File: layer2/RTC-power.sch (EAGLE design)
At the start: 15 parts, among them U1 DS3234, U2 MCP73831

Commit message: Initail board argment
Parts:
- removed C4: 4.7uF, SparkFun-Capacitors:4.7UF-6.3V-10%(0603)0603
- removed R4: 2.0k, SparkFun-Resistors:2.0KOHM1/10W5%(0603)
- added C2: 4.7uF, microbuilder:CAP_CERAMIC0805-NOOUTLINE
- C1: device SparkFun:CAP0402-CAP -> microbuilder:CAP_CERAMIC0805-NOOUTLINE
- C3: device SparkFun-Capacitors:4.7UF-6.3V-10%(0603)0603 -> microbuilder:CAP_CERAMIC0805-NOOUTLINE
- R1: value 10k -> 10K; device SparkFun:RESISTOR0402-RES -> microbuilder:RESISTOR_0805MP
- R2: value (none) -> 2.0k; device SparkFun-Resistors:RESISTORPTH-1/4W-VERT-KIT -> microbuilder:RESISTOR_0805MP
- R3: device SparkFun-Resistors:330OHM1/10W1%(0603) -> microbuilder:RESISTOR_0805MP
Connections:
- removed net VCC: C1.2, R1.1
- net +3V3: now also C1.1, R1.1
- net GND: now also C1.2, C2.2; no longer C1.1, C4.2, R4.2
- net N$3: now also R3.2; no longer R3.1
- net PROG: no longer R4.1
- net VIN: now also C2.1, R3.1; no longer C3.1, R3.2
- net V_RAW: now also C3.1; no longer C4.1
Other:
- moved on the sheet: C1, C3

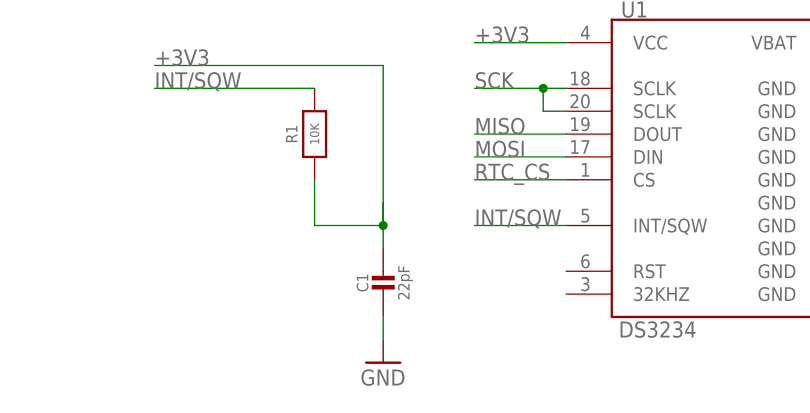
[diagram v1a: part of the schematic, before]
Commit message: layed out all conectons on board
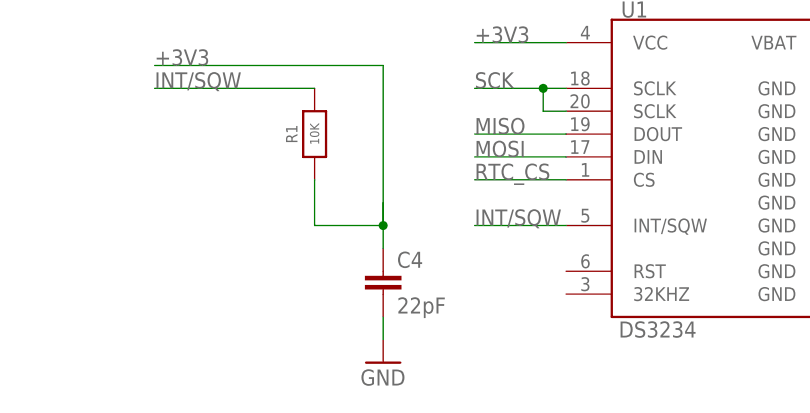
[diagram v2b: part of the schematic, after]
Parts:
- removed C1: 22pF, microbuilder:CAP_CERAMIC0805-NOOUTLINE
- added C4: 22pF, SparkFun:CAP0402-CAP
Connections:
- net +3V3: now also C4.1; no longer C1.1
- net GND: now also C4.2; no longer C1.2
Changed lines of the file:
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@@
 <part name="R3" library="microbuilder" deviceset="RESISTOR" device="_0805MP" value="330"/>
 <part name="R2" library="microbuilder" deviceset="RESISTOR" device="_0805MP" value="2.0k"/>
-<part name="C1" library="microbuilder" deviceset="CAP_CERAMIC" device="0805-NOOUTLINE" value="22pF"/>
 <part name="C2" library="microbuilder" deviceset="CAP_CERAMIC" device="0805-NOOUTLINE" value="4.7uF"/>
 <part name="C3" library="microbuilder" deviceset="CAP_CERAMIC" device="0805-NOOUTLINE" value="4.7uF"/>
+<part name="C4" library="SparkFun" deviceset="CAP" device="0402-CAP" value="22pF"/>
 </parts>
 <sheets>
@@
 <instance part="R3" gate="G$1" x="63.5" y="76.2" rot="R90"/>
 <instance part="R2" gate="G$1" x="93.98" y="76.2" rot="R90"/>
-<instance part="C1" gate="G$1" x="48.26" y="25.4"/>
 <instance part="C2" gate="G$1" x="48.26" y="91.44"/>
 <instance part="C3" gate="G$1" x="104.14" y="91.44"/>
+<instance part="C4" gate="G$1" x="48.26" y="25.4"/>
 </instances>
 <busses>
@@
 </segment>
 <segment>
-<pinref part="C1" gate="G$1" pin="2"/>
 <pinref part="GND2" gate="1" pin="GND"/>
 <wire x1="48.26" y1="22.86" x2="48.26" y2="20.32" width="0.1524" layer="91"/>
+<pinref part="C4" gate="G$1" pin="2"/>
 </segment>
 </net>
@@
 <label x="22.86" y="50.8" size="1.778" layer="95"/>
 <pinref part="R1" gate="G$1" pin="1"/>
-<pinref part="C1" gate="G$1" pin="1"/>
 <wire x1="48.26" y1="30.48" x2="48.26" y2="33.02" width="0.1524" layer="91"/>
-</segment>
-</net>
+<pinref part="C4" gate="G$1" pin="1"/>
+</segment>
+</net>

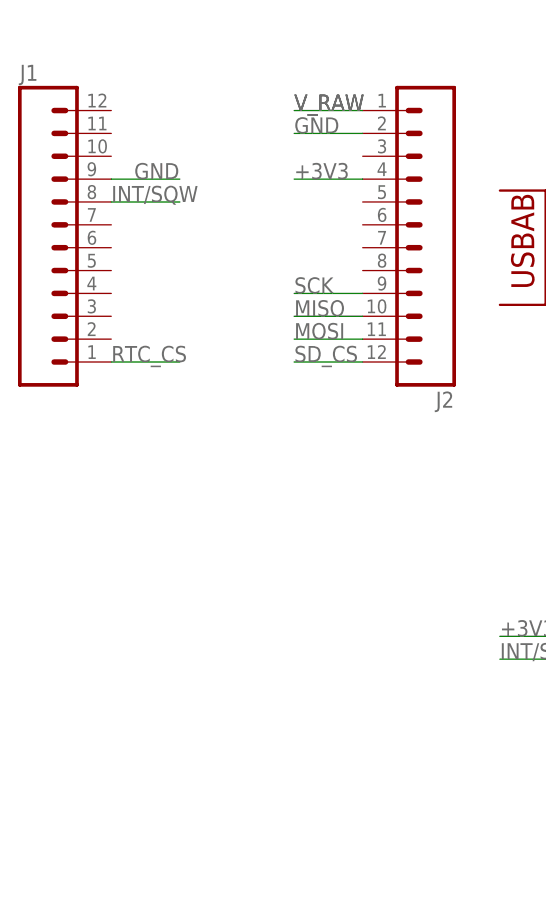
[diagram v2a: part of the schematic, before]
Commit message: removed unneeded header to give battery access
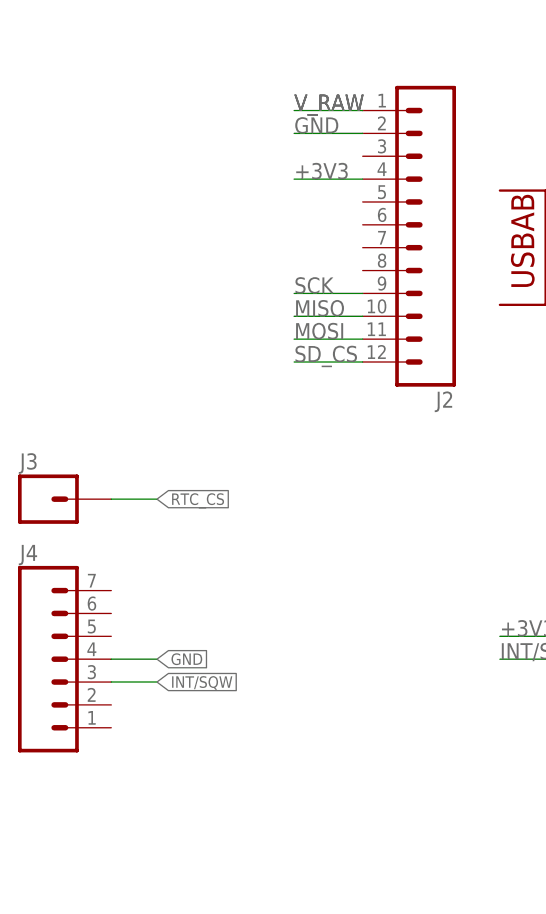
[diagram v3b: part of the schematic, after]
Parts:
- removed J1: (no value), SparkFun-Connectors:M12PTH
- added J3: (no value), SparkFun-Connectors:M01PTH
- added J4: (no value), SparkFun-Connectors:M07
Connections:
- net GND: now also J4.4; no longer J1.9
- net INT/SQW: now also J4.3; no longer J1.8
- net RTC_CS: now also J3.1; no longer J1.1
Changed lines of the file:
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@@
 <setting verticaltext="up"/>
 </settings>
-<grid distance="0.1" unitdist="inch" unit="inch" style="lines" multiple="1" display="no" altdistance="0.01" altunitdist="inch" altunit="inch"/>
+<grid distance="0.1" unitdist="inch" unit="inch" style="lines" multiple="1" display="yes" altdistance="0.01" altunitdist="inch" altunit="inch"/>
 <layers>
 <layer number="1" name="Top" color="4" fill="1" visible="no" active="no"/>
@@
 <part name="JP9" library="SparkFun-Connectors" deviceset="USB-AB" device="CONN-11794" value="Micro USB"/>
 <part name="JP1" library="SparkFun-Connectors" deviceset="JST_2MM_MALE" device="" value="JST"/>
-<part name="J1" library="SparkFun-Connectors" deviceset="M12" device="PTH"/>
 <part name="J2" library="SparkFun-Connectors" deviceset="M12" device="PTH"/>
 <part name="R1" library="microbuilder" deviceset="RESISTOR" device="_0805MP" value="10K"/>
@@
 <part name="C3" library="microbuilder" deviceset="CAP_CERAMIC" device="0805-NOOUTLINE" value="4.7uF"/>
 <part name="C4" library="SparkFun" deviceset="CAP" device="0402-CAP" value="22pF"/>
+<part name="J3" library="SparkFun-Connectors" deviceset="M01" device="PTH"/>
+<part name="J4" library="SparkFun-Connectors" deviceset="M07" device=""/>
 </parts>
 <sheets>
@@
 <instance part="JP9" gate="G$1" x="25.4" y="93.98" smashed="yes" rot="R180"/>
 <instance part="JP1" gate="G$1" x="116.84" y="106.68" rot="MR0"/>
-<instance part="J1" gate="G$1" x="-30.48" y="96.52"/>
 <instance part="J2" gate="G$1" x="17.78" y="93.98" rot="R180"/>
 <instance part="R1" gate="G$1" x="40.64" y="43.18" rot="R90"/>
@@
 <instance part="C3" gate="G$1" x="104.14" y="91.44"/>
 <instance part="C4" gate="G$1" x="48.26" y="25.4"/>
+<instance part="J3" gate="G$1" x="-27.94" y="66.04"/>
+<instance part="J4" gate="G$1" x="-25.4" y="45.72"/>
 </instances>
 <busses>
@@
 </segment>
 <segment>
-<wire x1="-20.32" y1="81.28" x2="-12.7" y2="81.28" width="0.1524" layer="91"/>
-<label x="-20.32" y="81.28" size="1.778" layer="95"/>
-<pinref part="J1" gate="G$1" pin="1"/>
+<pinref part="J3" gate="G$1" pin="1"/>
+<wire x1="-20.32" y1="66.04" x2="-15.24" y2="66.04" width="0.1524" layer="91"/>
+<label x="-15.24" y="66.04" size="1.27" layer="95" xref="yes"/>
 </segment>
 </net>
@@
 </segment>
 <segment>
-<wire x1="-20.32" y1="101.6" x2="-12.7" y2="101.6" width="0.1524" layer="91"/>
-<label x="-17.78" y="101.6" size="1.778" layer="95"/>
-<pinref part="J1" gate="G$1" pin="9"/>
-</segment>
-<segment>
 <wire x1="7.62" y1="106.68" x2="0" y2="106.68" width="0.1524" layer="91"/>
 <label x="0" y="106.68" size="1.778" layer="95"/>
@@
 <pinref part="C4" gate="G$1" pin="2"/>
 </segment>
+<segment>
+<pinref part="J4" gate="G$1" pin="4"/>
+<wire x1="-20.32" y1="48.26" x2="-15.24" y2="48.26" width="0.1524" layer="91"/>
+<label x="-15.24" y="48.26" size="1.27" layer="95" xref="yes"/>
+</segment>
 </net>
 <net name="MISO" class="0">
@@
 </segment>
 <segment>
-<wire x1="-20.32" y1="99.06" x2="-12.7" y2="99.06" width="0.1524" layer="91"/>
-<label x="-20.32" y="99.06" size="1.778" layer="95"/>
-<pinref part="J1" gate="G$1" pin="8"/>
-</segment>
-</net>
+<pinref part="J4" gate="G$1" pin="3"/>
+<wire x1="-20.32" y1="45.72" x2="-15.24" y2="45.72" width="0.1524" layer="91"/>
+<label x="-15.24" y="45.72" size="1.27" layer="95" xref="yes"/>
+</segment>
+</net>

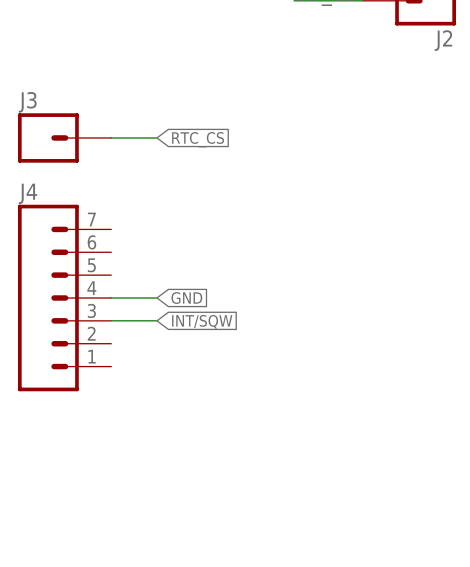
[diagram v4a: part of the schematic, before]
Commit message: removed pin 4, movved batt holder
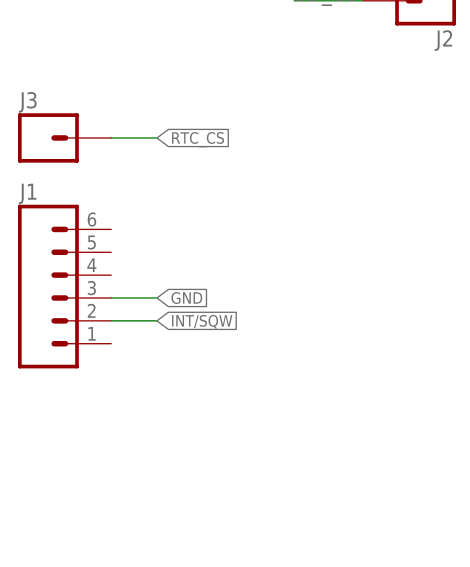
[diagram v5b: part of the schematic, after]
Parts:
- removed J4: (no value), SparkFun-Connectors:M07
- added J1: (no value), SparkFun-Connectors:M06SILK_FEMALE_PTH
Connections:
- net GND: no longer J4.4
- net INT/SQW: no longer J4.3
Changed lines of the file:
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@@
 <setting verticaltext="up"/>
 </settings>
-<grid distance="0.1" unitdist="inch" unit="inch" style="lines" multiple="1" display="no" altdistance="0.01" altunitdist="inch" altunit="inch"/>
+<grid distance="0.1" unitdist="inch" unit="inch" style="lines" multiple="1" display="yes" altdistance="0.01" altunitdist="inch" altunit="inch"/>
 <layers>
 <layer number="1" name="Top" color="4" fill="1" visible="no" active="no"/>
@@
 <part name="C4" library="SparkFun" deviceset="CAP" device="0402-CAP" value="22pF"/>
 <part name="J3" library="SparkFun-Connectors" deviceset="M01" device="PTH"/>
-<part name="J4" library="SparkFun-Connectors" deviceset="M07" device=""/>
+<part name="J1" library="SparkFun-Connectors" deviceset="M06" device="SILK_FEMALE_PTH"/>
 </parts>
 <sheets>
@@
 <instance part="C4" gate="G$1" x="48.26" y="25.4"/>
 <instance part="J3" gate="G$1" x="-27.94" y="66.04"/>
-<instance part="J4" gate="G$1" x="-25.4" y="45.72"/>
+<instance part="J1" gate="G$1" x="-25.4" y="48.26"/>
 </instances>
 <busses>
@@
 </segment>
 <segment>
-<pinref part="J4" gate="G$1" pin="4"/>
 <wire x1="-20.32" y1="48.26" x2="-15.24" y2="48.26" width="0.1524" layer="91"/>
 <label x="-15.24" y="48.26" size="1.27" layer="95" xref="yes"/>
@@
 </segment>
 <segment>
-<pinref part="J4" gate="G$1" pin="3"/>
 <wire x1="-20.32" y1="45.72" x2="-15.24" y2="45.72" width="0.1524" layer="91"/>
 <label x="-15.24" y="45.72" size="1.27" layer="95" xref="yes"/>
